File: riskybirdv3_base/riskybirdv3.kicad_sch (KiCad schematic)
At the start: 146 parts, among them IC1 PMW3901MB-TXQT, J1 Conn_02x10_Odd_Even, J10 Conn_01x05, J11 Conn_01x05, J13 Conn_02x12_Odd_Even_MountingP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, J2 Conn_01x05, J3 Conn_01x02, J4 Conn_01x02, J5 Conn_01x02, J6 Conn_01x02, J7 Conn_01x02, J8 USB_B_Micro, J9 Conn_01x05, Q1 SI2302, Q2 SI2302, Q3 SI2302, Q4 SI2302, Q5 AON7407, SW1 SW_SPST, SW2 SW_SPST, SW4 SW_SPST, SW5 SW_SPST, U1 ADS7128IRTER, U10 TLV70018DCKR, U11 TLV70015DCKT, U14 ESP32-C6-MINI-1/U, U2 LTC3119EUFD#TRPBF, U3 BMI088, U4 MCP73831-2-OT, U7 TLV70028DCKR, U8 TPS2117DRLR_C22399676, U9 VL53L1CXV0FY1

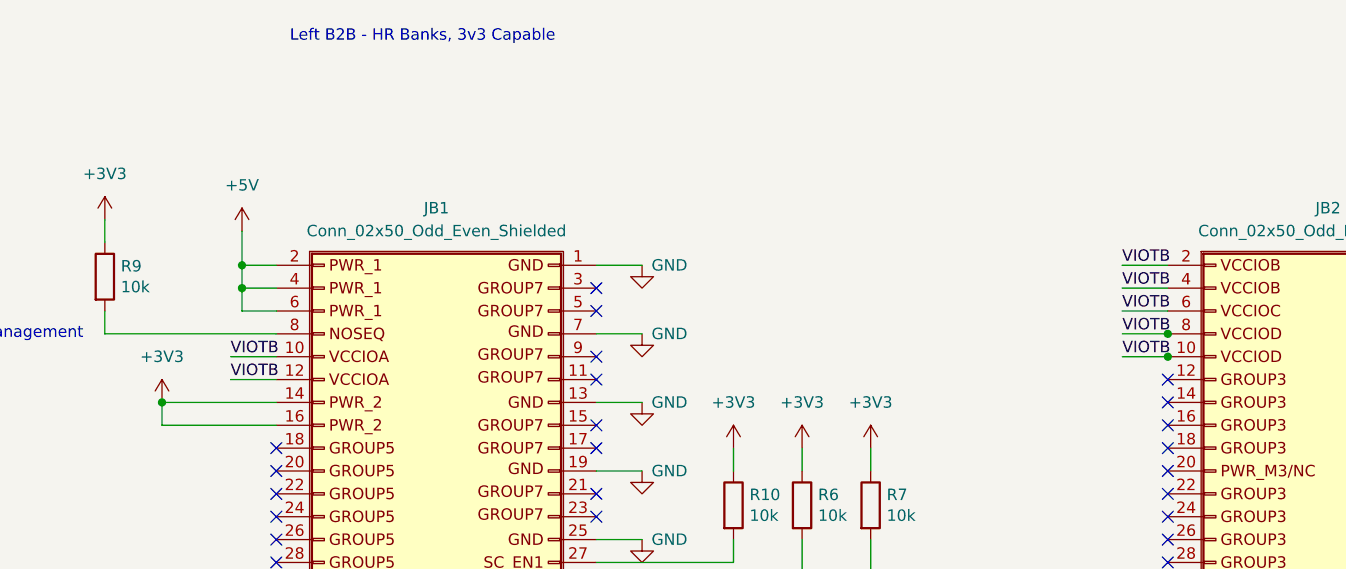
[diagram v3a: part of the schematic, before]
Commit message: fix: split power domains for b2bs
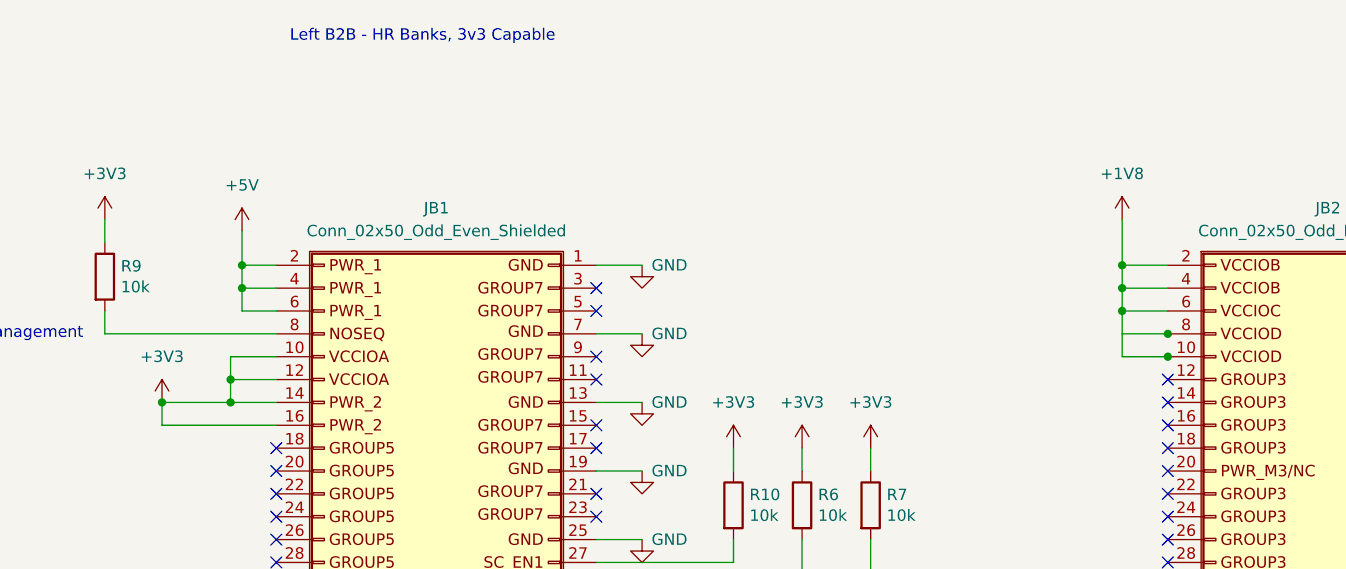
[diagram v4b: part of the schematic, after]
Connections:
- net +1V8: now also JB2.2 (Pin_2), JB2.4 (Pin_4), JB2.6 (Pin_6)
- net +3V3: now also JB1.10 (Pin_10), JB1.12 (Pin_12)
- removed net VIOTB: JB1.10 (Pin_10), JB1.12 (Pin_12), JB2.10 (Pin_10), JB2.2 (Pin_2), JB2.4 (Pin_4), JB2.6 (Pin_6), JB2.8 (Pin_8)
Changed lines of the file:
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@@
 	)
 	(junction
+		(at 668.02 48.26)
+		(diameter 0)
+		(color 0 0 0 0)
+	)
+	(junction
+		(at 668.02 50.8)
+		(diameter 0)
+		(color 0 0 0 0)
+	)
+	(junction
 		(at 207.01 147.32)
 		(diameter 0)
@@
 	)
 	(junction
+		(at 767.08 40.64)
+		(diameter 0)
+		(color 0 0 0 0)
+	)
+	(junction
 		(at 50.8 223.52)
 		(diameter 0)
@@
 	)
 	(junction
+		(at 767.08 35.56)
+		(diameter 0)
+		(color 0 0 0 0)
+	)
+	(junction
 		(at 189.23 341.63)
 		(diameter 0)
@@
 	)
 	(junction
+		(at 767.08 38.1)
+		(diameter 0)
+		(color 0 0 0 0)
+	)
+	(junction
 		(at 88.9 113.03)
 		(diameter 0)
@@
 	(wire
 		(pts
+			(xy 767.08 40.64) (xy 767.08 45.72)
+		)
+		(stroke
+			(width 0)
+			(type default)
+		)
+	)
+	(wire
+		(pts
 			(xy 40.64 386.08) (xy 43.18 386.08)
 		)
@@
 		)
 	)
+	(wire
+		(pts
+			(xy 767.08 30.48) (xy 767.08 35.56)
+		)
+		(stroke
+			(width 0)
+			(type default)
+		)
+	)
 	(polyline
 		(pts
@@
 	(wire
 		(pts
+			(xy 668.02 48.26) (xy 668.02 50.8)
+		)
+		(stroke
+			(width 0)
+			(type default)
+		)
+	)
+	(wire
+		(pts
 			(xy 302.26 30.48) (xy 308.61 30.48)
 		)
@@
 	(wire
 		(pts
+			(xy 668.02 45.72) (xy 668.02 48.26)
+		)
+		(stroke
+			(width 0)
+			(type default)
+		)
+	)
+	(wire
+		(pts
 			(xy 822.96 55.88) (xy 822.96 54.61)
 		)
@@
 	(wire
 		(pts
+			(xy 668.02 50.8) (xy 660.4 50.8)
+		)
+		(stroke
+			(width 0)
+			(type default)
+		)
+	)
+	(wire
+		(pts
 			(xy 902.97 88.9) (xy 908.05 88.9)
 		)
@@
 	(wire
 		(pts
-			(xy 673.1 50.8) (xy 660.4 50.8)
+			(xy 673.1 50.8) (xy 668.02 50.8)
 		)
 		(stroke
@@
 	(wire
 		(pts
+			(xy 767.08 35.56) (xy 767.08 38.1)
+		)
+		(stroke
+			(width 0)
+			(type default)
+		)
+	)
+	(wire
+		(pts
 			(xy 91.44 163.83) (xy 118.11 163.83)
 		)
@@
 	(wire
 		(pts
+			(xy 767.08 38.1) (xy 767.08 40.64)
+		)
+		(stroke
+			(width 0)
+			(type default)
+		)
+	)
+	(wire
+		(pts
 			(xy -100.33 303.53) (xy -88.9 303.53)
 		)
@@
 		)
 	)
-	(label "VIOTB"
-		(at 668.02 45.72 0)
-		(effects
-			(font
-				(size 1.27 1.27)
-			)
-			(justify left bottom)
-		)
-	)
 	(label "RV_TCK"
 		(at 723.9 91.44 0)
@@
 		)
 	)
-	(label "VIOTB"
-		(at 767.08 40.64 0)
-		(effects
-			(font
-				(size 1.27 1.27)
-			)
-			(justify left bottom)
-		)
-	)
 	(label "GPIO5"
 		(at 156.21 156.21 0)
@@
 		)
 	)
-	(label "VIOTB"
-		(at 668.02 48.26 0)
-		(effects
-			(font
-				(size 1.27 1.27)
-			)
-			(justify left bottom)
-		)
-	)
 	(label "SCLK"
 		(at 264.16 130.81 0)
@@
 		)
 	)
-	(label "VIOTB"
-		(at 767.08 38.1 0)
-		(effects
-			(font
-				(size 1.27 1.27)
-			)
-			(justify left bottom)
-		)
-	)
 	(label "NCS"
 		(at -21.59 191.77 0)
@@
 		)
 	)
-	(label "VIOTB"
-		(at 767.1038 43.18 0)
-		(effects
-			(font
-				(size 1.27 1.27)
-			)
-			(justify left bottom)
-		)
-	)
 	(label "D0"
 		(at 400.05 262.89 0)
@@
 		)
 	)
-	(label "VIOTB"
-		(at 767.08 35.56 0)
-		(effects
-			(font
-				(size 1.27 1.27)
-			)
-			(justify left bottom)
-		)
-	)
 	(label "RST"
 		(at 156.21 29.21 0)
@@
 		)
 	)
-	(label "VIOTB"
-		(at 767.1038 45.72 0)
-		(effects
-			(font
-				(size 1.27 1.27)
-			)
-			(justify left bottom)
-		)
-	)
 	(label "SDA"
 		(at 124.46 104.14 0)
@@
 					(unit 1)
 				)
+			)
+		)
+	)
+	(symbol
+		(lib_id "power:+1V8")
+		(at 767.08 30.48 0)
+		(unit 1)
+		(body_style 1)
+		(exclude_from_sim no)
+		(in_bom yes)
+		(on_board yes)
+		(in_pos_files yes)
+		(dnp no)
+		(fields_autoplaced yes)
+		(property "Reference" "#PWR056"
+			(at 767.08 34.29 0)
+			(hide yes)
+			(show_name no)
+			(do_not_autoplace no)
+			(effects
+				(font
+					(size 1.27 1.27)
+				)
+			)
+		)
+		(property "Value" "+1V8"
+			(at 767.08 25.4 0)
+			(show_name no)
+			(do_not_autoplace no)
+			(effects
+				(font
+					(size 1.27 1.27)
+				)
+			)
+		)
+		(property "Footprint" ""
+			(at 767.08 30.48 0)
+			(hide yes)
+			(show_name no)
+			(do_not_autoplace no)
+			(effects
+				(font
+					(size 1.27 1.27)
+				)
+			)
+		)
+		(property "Datasheet" ""
+			(at 767.08 30.48 0)
+			(hide yes)
+			(show_name no)
+			(do_not_autoplace no)
+			(effects
+				(font
+					(size 1.27 1.27)
+				)
+			)
+		)
+		(property "Description" "Power symbol creates a global label with name \"+1V8\""
+			(at 767.08 30.48 0)
+			(hide yes)
+			(show_name no)
+			(do_not_autoplace no)
+			(effects
+				(font
+					(size 1.27 1.27)
+				)
+			)
+		)
+		(pin "1"
+		)
+		(instances
+			(project "riskybirdv3"
+				(path "/b045bc91-b5c2-4b45-9ee6-c32404600013"
+					(reference "#PWR056")
+					(unit 1)
+				)

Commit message: riskybirdv3: PMW3901 fixes (motor3 R, LED_N NC unroute, CamRST pull-up) + board
- Add missing MOTOR3 FPGA-leg series resistor (was ESP-only).
- Unroute PMW3901 pin 20 (datasheet NC; symbol mislabels it LED_N).
- CamRST/NRESET: add 47k pull-up to +3V3 (defaults sensor to running).
- Board (.kicad_pcb) current state.

TODO (power, next): SoM VIN wired to +5V (USB-only) -> must be +3V3;
B66_VCCO (bank 66 HP, JB3) not supplied; buck-boost size for >=4A SoM;
verify /VBAT -> JB1.80.
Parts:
- removed R11, R5: Poka Yoke UART, symbol poka_yoke_uart:Poka Yoke UART
- added R21, R24, R26, R27, R28, R29, R34, R38: 47R, Resistor_SMD:R_0201_0603Metric, symbol Device:R
- added R37: 47k, Resistor_SMD:R_0201_0603Metric, symbol Device:R
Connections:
- net +3V3: now also R37.1
- net CamRST: now also R37.2; no longer JB2.71 (Pin_71), U14.5 (GPIO2/ADC1_CH2)
- net LED_N: no longer JB2.75 (Pin_75), U14.6 (GPIO3/ADC1_CH3)
- net MISO: now also R28.2; no longer JB2.63 (Pin_63)
- net MOSI: now also R29.2; no longer JB2.65 (Pin_65)
- net MOTOR1: now also R24.1; no longer JB1.32 (Pin_32)
- net MOTOR2: now also R21.2; no longer JB1.35 (Pin_35)
- net MOTOR3: now also R38.1; no longer JB1.100 (Pin_80)
- net MOTOR4: now also R26.2; no longer JB1.99 (Pin_79)
- net NCS: now also R34.2; no longer JB2.67 (Pin_67)
- net RV_UART_RX: now also JB1.42 (Pin_42)
- net RV_UART_TX: now also JB1.44 (Pin_44)
- net SCLK: now also R27.2; no longer JB2.61 (Pin_61)
- net TSI_UART_RX: now also JB1.91 (Pin_71)
- net TSI_UART_TX: now also JB1.86 (Pin_66)
- new net: JB1.32 (Pin_32), R24.2
- new net: JB1.100 (Pin_80), R38.2
- new net: JB1.35 (Pin_35), R21.1
- new net: JB1.99 (Pin_79), R26.1
- new net: JB2.65 (Pin_65), R29.1
- new net: JB2.67 (Pin_67), R34.1
- new net: JB2.63 (Pin_63), R28.1
- new net: JB2.61 (Pin_61), R27.1
- no-connect marks 151 -> 152
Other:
- moved on the sheet: C37, C43, C46, C56, C58, R40, R51, R52, SW1, SW4

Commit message: riskybirdv3: USB-C+ESD, camera FPC/I2C level-shift, SoM B2B power/control, compact power switch
- ESP native USB-C (J8): USBLC6 ESD array on D+/D-, 5.1k CC pulldowns, HRO Type-C footprint
- U14 -> ESP32-C6-MINI-1U footprint (external U.FL antenna, no PCB-antenna keepout)
- HM01B0 camera (J13): DVP wiring + AVDD/IOVDD/DVDD rails; PCA9306 (U12) level-shifts 1.8V SCCB <-> shared 3.3V I2C
- SoM B2B (JB1/2/3): VIN/3.3VIN on +3V3, VCCIO banks, control pull-ups (EN1/JTAGSEL/NOSEQ/PGOOD/RESIN), JTAG data + VREF_JTAG(0R)
- SW3 -> MINI MSK12C02 slide switch (now only gates the P-FET, ~50uA)
- new footprints: ESP32-C6-MINI-1U, SW-SMD_MSK12CO2
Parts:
- removed J8: USB_B_Micro, Connector_USB:USB_Micro-B_Molex_47346-0001, symbol Connector:USB_B_Micro
- added C67, C73, C74, C75: 10u, Capacitor_SMD:C_0402_1005Metric, symbol Device:C
- added C68, C69, C70: 1u, Capacitor_SMD:C_0201_0603Metric, symbol Device:C
- added C71, C72: 0.1u, Capacitor_SMD:C_0402_1005Metric, symbol Device:C
- added J8: USB_C_Receptacle_USB2.0_16P, Connector_USB:USB_C_Receptacle_HRO_TYPE-C-31-M-12, symbol Connector:USB_C_Receptacle_USB2.0_16P
- added R11, R5: 5.1k, Resistor_SMD:R_0201_0603Metric, symbol Device:R
- added R39, R46: 0R, Resistor_SMD:R_0201_0603Metric, symbol Device:R
- added R67: 200k, Resistor_SMD:R_0201_0603Metric, symbol Device:R
- added R68, R69: 2.2k, Resistor_SMD:R_0201_0603Metric, symbol Device:R
- added U12: PCA9306DC, Package_SO:VSSOP-8_2.3x2mm_P0.5mm, symbol Interface:PCA9306DC
- added U6: USBLC6-2P6, Package_TO_SOT_SMD:SOT-666, symbol Power_Protection:USBLC6-2P6
- C44, C45, C50: footprint Capacitor_SMD:C_0402_1005Metric -> Capacitor_SMD:C_0201_0603Metric
- C62: value 0.1u -> 10u; footprint Capacitor_SMD:C_01005_0402Metric -> Capacitor_SMD:C_0402_1005Metric
- C63: value 0.1u -> 150u
- C64: footprint 470p -> Capacitor_SMD:C_0201_0603Metric
- C65: footprint Capacitor_SMD:C_0201_0603Metric -> Capacitor_SMD:C_0402_1005Metric
- SW5: footprint Button_Switch_SMD:SW_SPDT_CK_JS102011SAQN -> riskybird_lcsc:SW-SMD_MSK12CO2
- U14: footprint RF_Module:ESP32-C6-MINI-1 -> riskybird_lcsc:ESP32-C6-MINI-1U
- renumbered J13 to HM01B0_Conn1
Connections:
- net FLVD is gone; now on net FVLD: JB2.31 (Pin_31)
- net FPGA_VTREF is gone; now on net +3V3: J1.1 (Pin_1)
- net RV_VTREF is gone; now on net +3V3: J1.9 (Pin_9)
- net Some_Top_Reset is gone; now on net CHIP_EN: JB1.34 (Pin_34)
- net +1V5: now also C74.2
- net +1V8: now also JB2.10 (Pin_10), JB2.8 (Pin_8), C72.1, C73.2, R68.1, R69.1, U12.2 (VREF1)
- net +2V8: now also C75.2
- net +3V3: now also JB1.2 (Pin_2), JB1.4 (Pin_4), JB1.6 (Pin_6), JB2.1 (Pin_1), JB2.3 (Pin_3), JB2.5 (Pin_5), JB2.7 (Pin_7), C68.2, C69.2, C70.2, C71.1, R39.1, R67.1, U12.7 (VREF2)
- net +5V: now also J8.A4 (VBUS), J8.A9 (VBUS), J8.B4 (VBUS), J8.B9 (VBUS), U6.5 (VBUS); no longer JB1.2 (Pin_2), JB1.4 (Pin_4), JB1.6 (Pin_6), JB2.1 (Pin_1), JB2.3 (Pin_3), JB2.5 (Pin_5), JB2.7 (Pin_7)
- net GND: now also C67.2, C68.1, C69.1, C70.1, C71.2, C72.2, C73.1, C74.1, C75.1, J8.A1 (GND), J8.A12 (GND), J8.B1 (GND), J8.B12 (GND), J8.SH (SHIELD), R11.2, R46.1, R5.2, U12.1 (GND), U6.2 (GND)
- net SCL: now also JB1.57 (Pin_57), U12.6 (SCL2); no longer HM01B0_Conn1.7 (Pin_7), JB2.23 (Pin_23)
- net SDA: now also JB1.55 (Pin_55), U12.5 (SDA2); no longer HM01B0_Conn1.8 (Pin_8), JB2.21 (Pin_21)
- net USB_DN: now also U6.4 (I/O2)
- net USB_DP: now also U6.6 (I/O1)
- net VCOM: now also C67.1
- net at JB1.8 (Pin_8), R9.2: now also R46.2
- net FTDI_3v3_2: no longer names the net of JB2.92 (Pin_72)
- net FTDI_3v3_2: now also R39.2
- new net: J8.A5 (CC1), R11.1
- new net: R67.2, U12.8 (EN)
- new net: J8.A6 (D+), J8.B6 (D+), U6.1 (I/O1)
- new net: J8.A7 (D-), J8.B7 (D-), U6.3 (I/O2)
- new net: J8.B5 (CC2), R5.1
- new net CAM_SCL: HM01B0_Conn1.7 (Pin_7), R69.2, U12.3 (SCL1)
- new net CAM_SDA: HM01B0_Conn1.8 (Pin_8), R68.2, U12.4 (SDA1)
- no-connect marks 152 -> 153
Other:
- moved on the sheet: C1, D7, R2, R3, U4

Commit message: riskybirdv3: board placement/frame-rotation checkpoint + battery power-gating
- Board placement + H-frame rotation exploration (current placed state)
- Standby-drain gating: LED (D4) and battery-sense divider gated low-side via 2N7002 FETs (Q6/Q7) off VCOM -> zero drain when SW3 off
- Removed always-on ESP +BATT sense divider (R51/R52); battery sense moved to ADS7128 (U1)
- SW3 -> MINI MSK12C02 slide switch in place
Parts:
- removed R51: 200k, Resistor_SMD:R_0201_0603Metric, symbol Device:R
- removed R52: 100k, Resistor_SMD:R_0201_0603Metric, symbol Device:R
- added Q6, Q7: 2N7002, Package_TO_SOT_SMD:SOT-23, symbol Transistor_FET:2N7002
- added R47, R48: 200k, Resistor_SMD:R_0201_0603Metric, symbol Device:R_Small
- C14: footprint Capacitor_SMD:C_0201_0603Metric -> Capacitor_SMD:C_0402_1005Metric
- C51, C52, C53, C54, C55, C57: footprint Capacitor_SMD:C_0402_1005Metric -> Capacitor_SMD:C_0201_0603Metric
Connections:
- net +3V3: now also J1.10 (Pin_10), J1.2 (Pin_2); no longer J1.1 (Pin_1), J1.9 (Pin_9), R30.1
- net +BATT: now also R30.1
- net CHIP_EN: no longer JB1.34 (Pin_34)
- net FPGA_PROG_B: now also J1.7 (Pin_7); no longer J1.8 (Pin_8)
- net FPGA_TCK: now also J1.4 (Pin_4); no longer J1.3 (Pin_3)
- net FPGA_TDI: now also J1.8 (Pin_8); no longer J1.7 (Pin_7)
- net FPGA_TDO: now also J1.5 (Pin_5); no longer J1.6 (Pin_6)
- net FPGA_TMS: now also J1.6 (Pin_6); no longer J1.5 (Pin_5)
- net GND: now also J1.1 (Pin_1), J1.11 (Pin_11), J1.19 (Pin_19), J1.3 (Pin_3), Q6.2 (S), Q7.2 (S), R47.2, R48.2; no longer D4.1 (K), J1.12 (Pin_12), J1.2 (Pin_2), J1.20 (Pin_20), J1.4 (Pin_4), R31.2
- net RST: now also JB1.34 (Pin_34)
- net RV_TCK: now also J1.12 (Pin_12); no longer J1.11 (Pin_11)
- net RV_TDI: now also J1.13 (Pin_13); no longer J1.14 (Pin_14)
- net RV_TDO: now also J1.9 (Pin_9); no longer J1.10 (Pin_10)
- net RV_TMS: now also J1.14 (Pin_14); no longer J1.13 (Pin_13)
- net RV_TRST: now also J1.16 (Pin_16); no longer J1.15 (Pin_15)
- net RV_UART_RX: now also J1.18 (Pin_18); no longer J1.17 (Pin_17)
- net RV_UART_TX: now also J1.15 (Pin_15); no longer J1.16 (Pin_16)
- net TSI_UART_RX: now also J1.20 (Pin_20); no longer J1.19 (Pin_19)
- net TSI_UART_TX: now also J1.17 (Pin_17); no longer J1.18 (Pin_18)
- net VCOM: now also Q6.1 (G), Q7.1 (G), R47.1, R48.1
- net VSENSE: no longer names the net of U14.12 (GPIO0/ADC1_CH0/XTAL_32K_P)
- new net: Q6.3 (D), R31.2
- new net: D4.1 (K), Q7.3 (D)
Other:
- moved on the sheet: D1, D4, R1, R12

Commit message: riskybirdv3: route power/signal nets — USB diff-pair swap, buck-boost bottom-layer zones, battery→motor power, GND/3V3 pours; all nets connected
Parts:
- added R70: 0R, Resistor_SMD:R_1206_3216Metric, symbol Device:R
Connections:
- net D0: now also JB3.37 (Pin_37); no longer JB2.41 (Pin_41)
- net D1: now also JB3.53 (Pin_53); no longer JB2.43 (Pin_43)
- net D2: now also JB3.39 (Pin_39); no longer JB2.45 (Pin_45)
- net D3: now also JB3.51 (Pin_51); no longer JB2.47 (Pin_47)
- net D4: now also JB3.41 (Pin_41); no longer JB2.51 (Pin_51)
- net D5: now also JB3.49 (Pin_49); no longer JB2.53 (Pin_53)
- net D6: now also JB3.43 (Pin_43); no longer JB2.55 (Pin_55)
- net D7: now also JB3.47 (Pin_47); no longer JB2.57 (Pin_57)
- net FVLD: now also JB3.40 (Pin_40); no longer JB2.31 (Pin_31)
- net INT: now also JB3.38 (Pin_38); no longer JB2.27 (Pin_27)
- net INT_BARO: now also JB1.50 (Pin_50); no longer JB1.52 (Pin_52)
- net LVLD: now also JB3.44 (Pin_44); no longer JB2.35 (Pin_35)
- net MCLK: now also JB3.58 (Pin_58); no longer JB2.33 (Pin_33)
- net MOSI: now also R34.2; no longer R29.2
- net NCS: now also R27.2; no longer R34.2
- net PCLK: now also JB3.57 (Pin_57); no longer JB2.37 (Pin_37)
- net SCLK: now also R29.2; no longer R27.2
- net TOF_Int: now also JB1.52 (Pin_52); no longer JB1.50 (Pin_50)
- net TRIG: now also JB3.42 (Pin_42); no longer JB2.25 (Pin_25)
- net TSI_UART_RX: now also JB3.60 (Pin_60); no longer JB1.91 (Pin_71)
- net TSI_UART_TX: now also JB3.59 (Pin_59); no longer JB1.86 (Pin_66)
- net U0RXD: now also JB1.97 (Pin_77)
- net U0TXD: now also JB1.95 (Pin_75)
- net at C61.2, L4.2, U2.5 (SW2): now also R70.1; no longer U2.2 (SW2)
- net CONN_DP: now reaches J8.A6 (D+), J8.B6 (D+), U6.1 (I/O1)
- net CONN_DN: now reaches J8.A7 (D-), J8.B7 (D-), U6.3 (I/O2)
- new net: R70.2, U2.2 (SW2)
- no-connect marks 153 -> 135
